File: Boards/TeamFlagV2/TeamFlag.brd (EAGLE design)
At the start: 46.2 x 47.5 mm, 11 parts

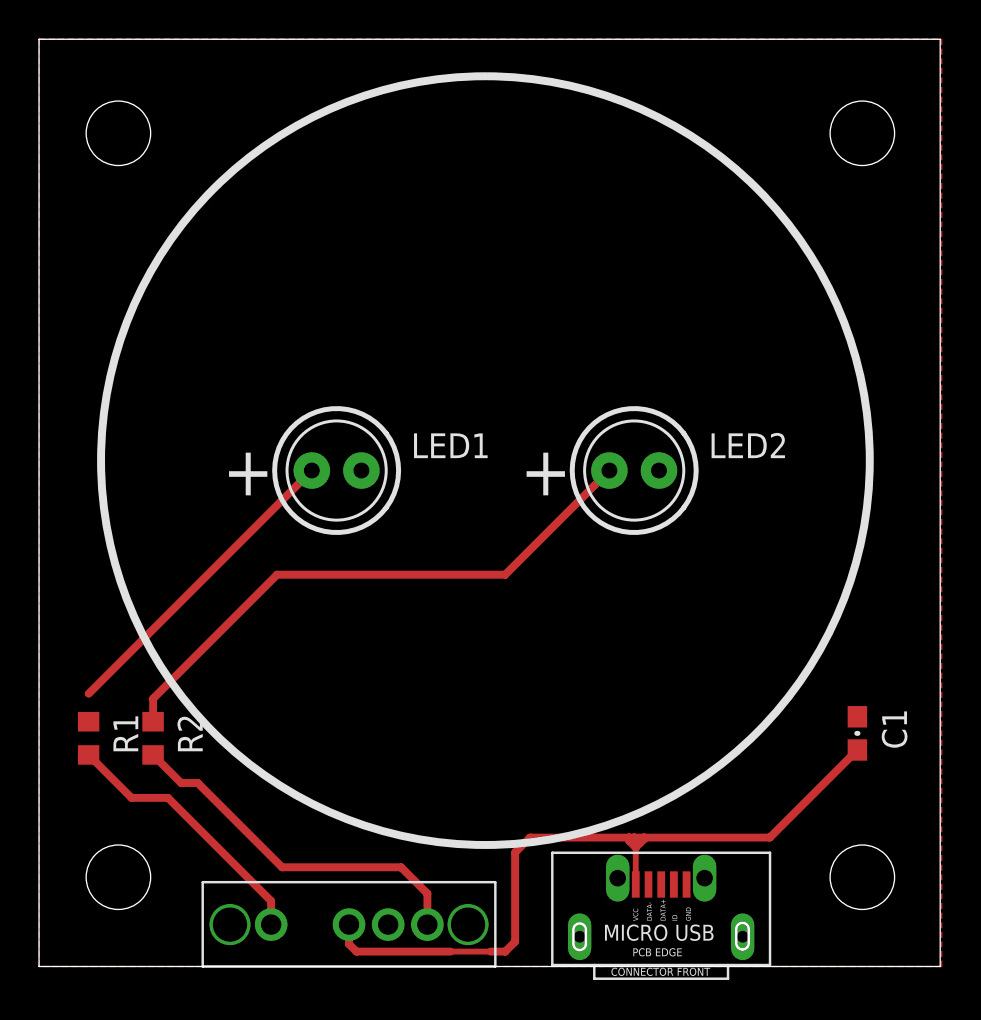
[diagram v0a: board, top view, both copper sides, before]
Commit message: Fixed board with new part updates
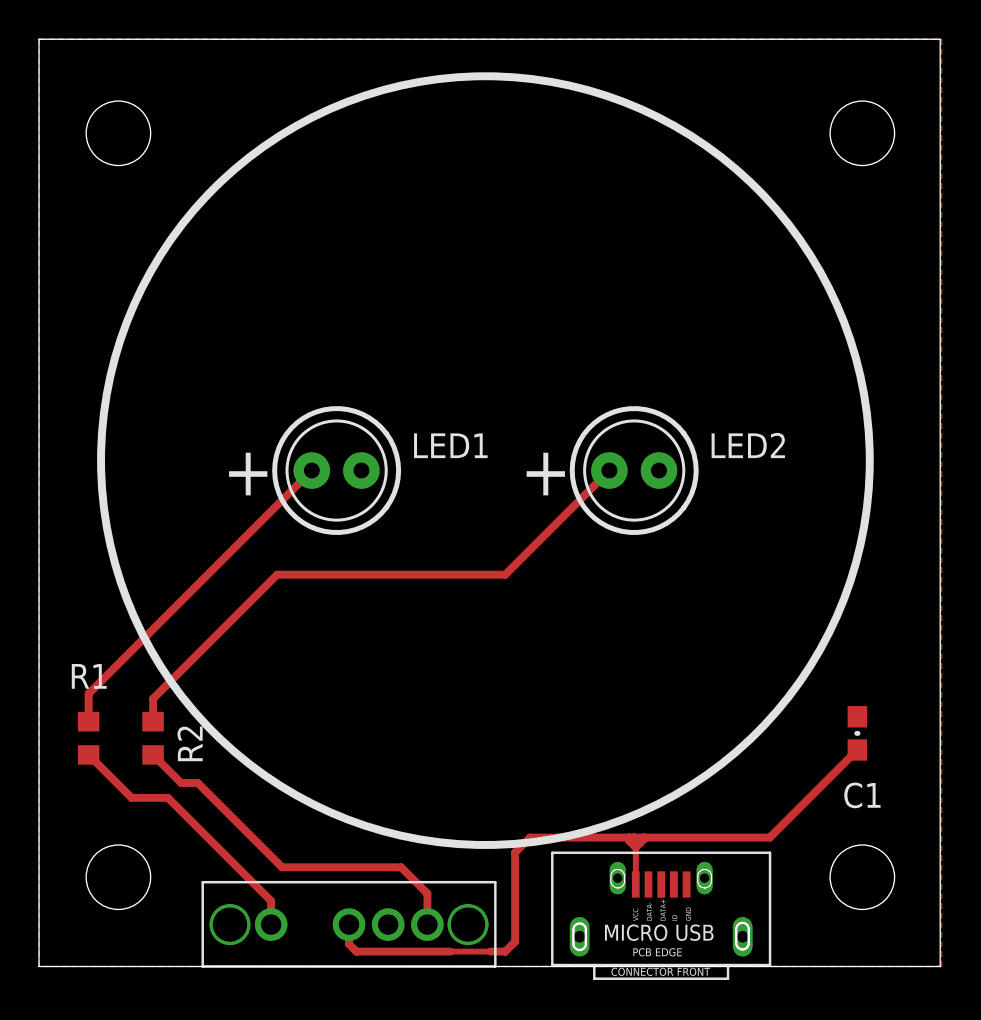
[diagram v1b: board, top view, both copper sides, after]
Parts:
- added U$7: (no value), pie:PIE-LOGO-SMALL
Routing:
- net N$2: track 16.2 -> 17.6 mm
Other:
- board text added: "(c) Pioneers In Engineering Design by: YOUR_NAMES_HERE This design is open source hardware. For more information, visit: https://github.com/pioneers/PiElectrical"
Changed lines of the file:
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@@
 <layer number="27" name="tValues" color="7" fill="1" visible="yes" active="yes"/>
 <layer number="28" name="bValues" color="7" fill="1" visible="yes" active="yes"/>
-<layer number="29" name="tStop" color="7" fill="3" visible="no" active="yes"/>
-<layer number="30" name="bStop" color="7" fill="6" visible="no" active="yes"/>
-<layer number="31" name="tCream" color="7" fill="4" visible="no" active="yes"/>
-<layer number="32" name="bCream" color="7" fill="5" visible="no" active="yes"/>
-<layer number="33" name="tFinish" color="6" fill="3" visible="no" active="yes"/>
-<layer number="34" name="bFinish" color="6" fill="6" visible="no" active="yes"/>
-<layer number="35" name="tGlue" color="7" fill="4" visible="no" active="yes"/>
-<layer number="36" name="bGlue" color="7" fill="5" visible="no" active="yes"/>
-<layer number="37" name="tTest" color="7" fill="1" visible="no" active="yes"/>
-<layer number="38" name="bTest" color="7" fill="1" visible="no" active="yes"/>
+<layer number="29" name="tStop" color="7" fill="3" visible="yes" active="yes"/>
+<layer number="30" name="bStop" color="7" fill="6" visible="yes" active="yes"/>
+<layer number="31" name="tCream" color="7" fill="4" visible="yes" active="yes"/>
+<layer number="32" name="bCream" color="7" fill="5" visible="yes" active="yes"/>
+<layer number="33" name="tFinish" color="6" fill="3" visible="yes" active="yes"/>
+<layer number="34" name="bFinish" color="6" fill="6" visible="yes" active="yes"/>
+<layer number="35" name="tGlue" color="7" fill="4" visible="yes" active="yes"/>
+<layer number="36" name="bGlue" color="7" fill="5" visible="yes" active="yes"/>
+<layer number="37" name="tTest" color="7" fill="1" visible="yes" active="yes"/>
+<layer number="38" name="bTest" color="7" fill="1" visible="yes" active="yes"/>
 <layer number="39" name="tKeepout" color="4" fill="11" visible="yes" active="yes"/>
 <layer number="40" name="bKeepout" color="1" fill="11" visible="yes" active="yes"/>
@@
 <layer number="42" name="bRestrict" color="1" fill="10" visible="yes" active="yes"/>
 <layer number="43" name="vRestrict" color="2" fill="10" visible="yes" active="yes"/>
-<layer number="44" name="Drills" color="7" fill="1" visible="no" active="yes"/>
+<layer number="44" name="Drills" color="7" fill="1" visible="yes" active="yes"/>
 <layer number="45" name="Holes" color="7" fill="1" visible="yes" active="yes"/>
-<layer number="46" name="Milling" color="3" fill="1" visible="no" active="yes"/>
-<layer number="47" name="Measures" color="7" fill="1" visible="no" active="yes"/>
+<layer number="46" name="Milling" color="3" fill="1" visible="yes" active="yes"/>
+<layer number="47" name="Measures" color="7" fill="1" visible="yes" active="yes"/>
 <layer number="48" name="Document" color="7" fill="1" visible="yes" active="yes"/>
 <layer number="49" name="Reference" color="7" fill="1" visible="yes" active="yes"/>
@@
 Team Flag
 Rev 10A</text>
+<text x="43.942" y="17.018" size="1.778" layer="22" rot="MR0">(c) Pioneers In Engineering
+Design by: YOUR_NAMES_HERE
+This design is open source hardware.
+For more information, visit:
+https://github.com/pioneers/PiElectrical</text>
 </plain>
 <attributes>
@@
 </autorouter>
 <elements>
-<element name="C1" library="pie" package="0603-CAP" value="0.1uF" x="41.91" y="11.938" rot="R270">
+<element name="C1" library="pie" package="0603-CAP" value="0.1uF" x="41.91" y="11.938" smashed="yes" rot="R270">
 <attribute name="PIE-INT-REF-NUM" value="CAPACITOR-GENERIC" x="41.91" y="11.938" size="1.778" layer="27" rot="R270" display="off"/>
+<attribute name="NAME" x="41.148" y="8.128" size="1.27" layer="25" font="vector" ratio="10"/>
+<attribute name="VALUE" x="40.386" y="14.478" size="1.27" layer="27" font="vector"/>
 </element>
 <element name="LED1" library="pie" package="LED5MM-NOFLAT" value="Yellow" x="15.24" y="25.4">
@@
 <attribute name="PIE-INT-REF-NUM" value="LED" x="30.48" y="25.4" size="1.778" layer="27" display="off"/>
 </element>
-<element name="R1" library="pie" package="R0603" value="130" x="2.54" y="11.684" rot="R270">
+<element name="R1" library="pie" package="R0603" value="130" x="2.54" y="11.684" smashed="yes" rot="R270">
 <attribute name="MANUFACTURER_PART_NUMBER" value="" x="2.54" y="11.684" size="1.778" layer="27" rot="R270" display="off"/>
 <attribute name="NOTES" value="Cut Tape" x="2.54" y="11.684" size="1.778" layer="27" rot="R270" display="off"/>
@@
 <attribute name="DISTRIBUTOR_PART_NUMBER" value="" x="2.54" y="11.684" size="1.778" layer="27" rot="R270" display="off"/>
 <attribute name="MANUFACTURER" value="Rohm Semiconductor" x="2.54" y="11.684" size="1.778" layer="27" rot="R270" display="off"/>
-</element>
-<element name="R2" library="pie" package="R0603" value="130" x="5.842" y="11.684" rot="R270">
+<attribute name="NAME" x="1.524" y="14.224" size="1.27" layer="25" font="vector" ratio="10"/>
+<attribute name="VALUE" x="0.762" y="8.128" size="1.27" layer="27" font="vector"/>
+</element>
+<element name="R2" library="pie" package="R0603" value="130" x="5.842" y="11.684" smashed="yes" rot="R270">
 <attribute name="MANUFACTURER_PART_NUMBER" value="" x="5.842" y="11.684" size="1.778" layer="27" rot="R270" display="off"/>
 <attribute name="NOTES" value="Cut Tape" x="5.842" y="11.684" size="1.778" layer="27" rot="R270" display="off"/>
@@
 <attribute name="DISTRIBUTOR_PART_NUMBER" value="" x="5.842" y="11.684" size="1.778" layer="27" rot="R270" display="off"/>
 <attribute name="MANUFACTURER" value="Rohm Semiconductor" x="5.842" y="11.684" size="1.778" layer="27" rot="R270" display="off"/>
+<attribute name="NAME" x="7.112" y="12.446" size="1.27" layer="25" font="vector" ratio="10" rot="R270"/>
+<attribute name="VALUE" x="4.572" y="8.128" size="1.27" layer="27" font="vector"/>
 </element>
 <element name="U$1" library="pie" package="MICRO_USB" value="MICRO_USB" x="27.686" y="1.524"/>
@@
 <element name="U$6" library="pie" package="STAND-OFF" value="" x="42.164" y="4.572"/>
 <element name="U$2" library="pie" package="SP3T_SLIDE_SWITCH" value="SP3T_SLIDE_SWITCH" x="8.382" y="0"/>
+<element name="U$7" library="pie" package="PIE-LOGO-SMALL" value="" x="23.622" y="12.192" rot="MR0"/>
 </elements>
 <signals>
@@
 <contactref element="R1" pad="1"/>
 <contactref element="LED1" pad="A"/>
-<wire x1="2.54" y1="12.534" x2="2.54" y2="13.97" width="0" layer="19" extent="1-16"/>
 <wire x1="2.54" y1="13.97" x2="13.97" y2="25.4" width="0.4064" layer="1"/>
+<wire x1="2.54" y1="12.534" x2="2.54" y2="13.97" width="0.4064" layer="1"/>
 </signal>
 <signal name="N$3">

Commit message: Appeasing the master
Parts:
- moved U$7 3.45 mm to (22.6, 15.5)
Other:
- board text added: "(c) Pioneers In Engineering Design by: Averal K, Nick W This design is open source hardware. For more information, visit: https://github.com/pioneers/PiElectrical"
- board text removed: "(c) Pioneers In Engineering Design by: YOUR_NAMES_HERE This design is open source hardware. For more information, visit: https://github.com/pioneers/PiElectrical"
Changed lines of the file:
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@@
 Team Flag
 Rev 10A</text>
-<text x="43.942" y="17.018" size="1.778" layer="22" rot="MR0">(c) Pioneers In Engineering
-Design by: YOUR_NAMES_HERE
+<text x="35.052" y="23.114" size="0.8128" layer="22" font="vector" rot="MR0">(c) Pioneers In Engineering
+Design by: Averal K, Nick W
 This design is open source hardware.
 For more information, visit:
@@
 <element name="U$6" library="pie" package="STAND-OFF" value="" x="42.164" y="4.572"/>
 <element name="U$2" library="pie" package="SP3T_SLIDE_SWITCH" value="SP3T_SLIDE_SWITCH" x="8.382" y="0"/>
-<element name="U$7" library="pie" package="PIE-LOGO-SMALL" value="" x="23.622" y="12.192" rot="MR0"/>
+<element name="U$7" library="pie" package="PIE-LOGO-SMALL" value="" x="22.606" y="15.494" rot="MR0"/>
 </elements>
 <signals>

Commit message: swag
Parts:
- moved U$7 3.59 mm to (22.1, 11.9)
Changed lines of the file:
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@@
 Team Flag
 Rev 10A</text>
-<text x="35.052" y="23.114" size="0.8128" layer="22" font="vector" rot="MR0">(c) Pioneers In Engineering
+<text x="34.29" y="16.002" size="0.8128" layer="22" font="vector" rot="MR0">(c) Pioneers In Engineering
 Design by: Averal K, Nick W
 This design is open source hardware.
@@
 <element name="U$6" library="pie" package="STAND-OFF" value="" x="42.164" y="4.572"/>
 <element name="U$2" library="pie" package="SP3T_SLIDE_SWITCH" value="SP3T_SLIDE_SWITCH" x="8.382" y="0"/>
-<element name="U$7" library="pie" package="PIE-LOGO-SMALL" value="" x="22.606" y="15.494" rot="MR0"/>
+<element name="U$7" library="pie" package="PIE-LOGO-SMALL" value="" x="22.098" y="11.938" rot="MR0"/>
 </elements>
 <signals>

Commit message: Fix the routing issues
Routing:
- net VCC: track 37.9 -> 40.1 mm, vias 0 -> 1
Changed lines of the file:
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@@
 <?xml version="1.0" encoding="utf-8"?>
 <!DOCTYPE eagle SYSTEM "eagle.dtd">
-<eagle version="8.0.0">
+<eagle version="7.6.0">
 <drawing>
 <settings>
@@
 <attribute name="DISTRIBUTOR_PART_NUMBER" value="" x="5.842" y="11.684" size="1.778" layer="27" rot="R270" display="off"/>
 <attribute name="MANUFACTURER" value="Rohm Semiconductor" x="5.842" y="11.684" size="1.778" layer="27" rot="R270" display="off"/>
-<attribute name="NAME" x="7.112" y="12.446" size="1.27" layer="25" font="vector" ratio="10" rot="R270"/>
+<attribute name="NAME" x="4.826" y="14.224" size="1.27" layer="25" font="vector" ratio="10"/>
 <attribute name="VALUE" x="4.572" y="8.128" size="1.27" layer="27" font="vector"/>
 </element>
@@
 <contactref element="U$2" pad="PIN2"/>
 <contactref element="U$1" pad="VCC"/>
-<wire x1="24.384" y1="5.842" x2="25.146" y2="6.604" width="0.4064" layer="1"/>
-<wire x1="25.146" y1="6.604" x2="30.226" y2="6.604" width="0.4064" layer="1"/>
-<wire x1="30.988" y1="6.604" x2="37.426" y2="6.604" width="0.4064" layer="1"/>
-<wire x1="37.426" y1="6.604" x2="41.91" y2="11.088" width="0.4064" layer="1"/>
-<wire x1="30.226" y1="6.604" x2="30.48" y2="6.604" width="0.4064" layer="1"/>
-<wire x1="30.48" y1="6.604" x2="30.988" y2="6.604" width="0.4064" layer="1"/>
-<wire x1="30.48" y1="6.604" x2="30.561" y2="6.523" width="0.4064" layer="1"/>
-<wire x1="30.561" y1="6.523" x2="30.561" y2="6.096" width="0.4064" layer="1"/>
-<wire x1="30.561" y1="6.096" x2="30.988" y2="6.523" width="0.4064" layer="1"/>
-<wire x1="30.988" y1="6.523" x2="30.988" y2="6.604" width="0.4064" layer="1"/>
-<wire x1="30.561" y1="6.096" x2="30.226" y2="6.431" width="0.4064" layer="1"/>
-<wire x1="30.226" y1="6.431" x2="30.226" y2="6.604" width="0.4064" layer="1"/>
-<wire x1="24.384" y1="1.27" x2="24.384" y2="5.842" width="0.4064" layer="1"/>
-<wire x1="23.876" y1="0.762" x2="24.384" y2="1.27" width="0.4064" layer="1"/>
-<wire x1="21.082" y1="0.762" x2="23.114" y2="0.762" width="0.3048" layer="1"/>
-<wire x1="23.114" y1="0.762" x2="23.876" y2="0.762" width="0.4064" layer="1"/>
-<wire x1="30.561" y1="6.096" x2="30.561" y2="4.199" width="0.3048" layer="1"/>
-<wire x1="15.875" y1="2.1463" x2="15.875" y2="1.143" width="0.4064" layer="1"/>
-<wire x1="15.875" y1="1.143" x2="16.256" y2="0.762" width="0.4064" layer="1"/>
-<wire x1="16.256" y1="0.762" x2="21.082" y2="0.762" width="0.4064" layer="1"/>
+<wire x1="15.875" y1="2.1463" x2="21.8567" y2="8.128" width="0.4064" layer="16"/>
+<wire x1="21.8567" y1="8.128" x2="23.368" y2="8.128" width="0.4064" layer="16"/>
+<via x="23.368" y="8.128" extent="1-16" drill="0.6" shape="square"/>
+<wire x1="23.368" y1="8.128" x2="26.328" y2="11.088" width="0.4064" layer="1"/>
+<wire x1="26.328" y1="11.088" x2="41.91" y2="11.088" width="0.4064" layer="1"/>
+<wire x1="30.561" y1="4.199" x2="30.561" y2="6.777" width="0.4064" layer="1"/>
+<wire x1="30.561" y1="6.777" x2="29.21" y2="8.128" width="0.4064" layer="1"/>
+<wire x1="29.21" y1="8.128" x2="23.368" y2="8.128" width="0.4064" layer="1"/>
 </signal>
 <signal name="PIN4">
